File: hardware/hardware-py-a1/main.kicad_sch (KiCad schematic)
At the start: 64 parts, among them J6 USB_C_Receptacle_USB2.0_16P, J7 Conn_02x08_Odd_Even, Q6 BSS138, SW1 SW_Push, SW10 SW_Push, SW11 SW_Push, SW12 SW_Push, SW13 SW_Push, SW14 SW_Push, SW15 SW_Push, SW16 SW_Push, SW17 SW_Push, SW18 SW_Push, SW19 SW_Push, SW2 SW_Push, SW20 SW_Push, SW21 Encoder, SW22 SW_Push, SW3 SW_Push, SW4 SW_Push, SW5 SW_Push, SW6 SW_Push, SW7 SW_Push, SW8 SW_Push, SW9 SW_Push, U3 74HC595, U4 ESP32-S3-WROOM-1

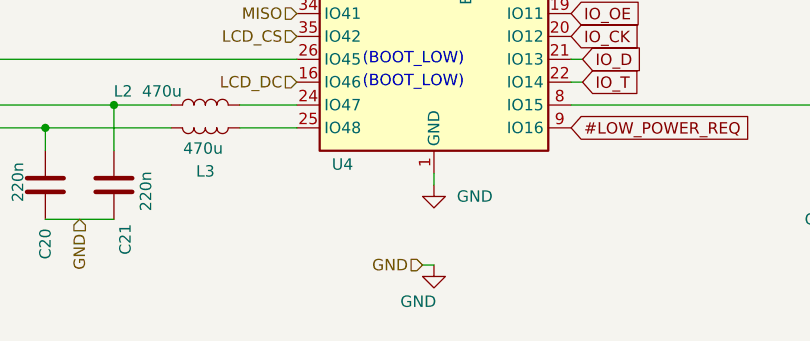
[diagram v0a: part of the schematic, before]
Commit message: hw: pya1 schematic rearange and post assembly test for inputs
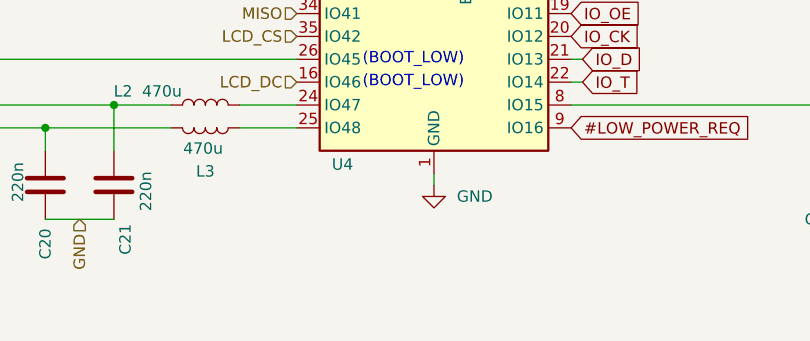
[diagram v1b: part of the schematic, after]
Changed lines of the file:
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@@
 	(wire
 		(pts
-			(xy 124.46 180.34) (xy 123.19 180.34)
-		)
-		(stroke
-			(width 0)
-			(type default)
-		)
-	)
-	(wire
-		(pts
 			(xy 228.6 59.69) (xy 232.41 59.69)
 		)
@@
 		)
 	)
-	(hierarchical_label "GND"
-		(shape input)
-		(at 123.19 180.34 180)
-		(effects
-			(font
-				(size 1.27 1.27)
-			)
-			(justify right)
-		)
-	)
 	(hierarchical_label "MOSI"
 		(shape input)
@@
 					(unit 1)
 				)
-			)
-		)
-	)
-	(symbol
-		(lib_id "power:GND")
-		(at 124.46 180.34 0)
-		(unit 1)
-		(exclude_from_sim no)
-		(in_bom yes)
-		(on_board yes)
-		(dnp no)
-		(property "Reference" "#PWR034"
-			(at 124.46 186.69 0)
-			(effects
-				(font
-					(size 1.27 1.27)
-				)
-				(hide yes)
-			)
-		)
-		(property "Value" "GND"
-			(at 124.714 184.404 0)
-			(effects
-				(font
-					(size 1.27 1.27)
-				)
-				(justify right)
-			)
-		)
-		(property "Footprint" ""
-			(at 124.46 180.34 0)
-			(effects
-				(font
-					(size 1.27 1.27)
-				)
-				(hide yes)
-			)
-		)
-		(property "Datasheet" ""
-			(at 124.46 180.34 0)
-			(effects
-				(font
-					(size 1.27 1.27)
-				)
-				(hide yes)
-			)
-		)
-		(property "Description" "Power symbol creates a global label with name \"GND\" , ground"
-			(at 124.46 180.34 0)
-			(effects
-				(font
-					(size 1.27 1.27)
-				)
-				(hide yes)
-			)
-		)
-		(pin "1"
-		)
-		(instances
-			(project "numcalcium"
-				(path "/842c0813-91d3-4f68-bc1f-ac3ce07be478/b6a1d74e-f5bd-4c1c-9567-b593baf30f34"
-					(reference "#PWR034")
-					(unit 1)
-				)
